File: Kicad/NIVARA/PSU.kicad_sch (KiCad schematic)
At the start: 0 parts

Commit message: Wrapping up for today :3
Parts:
- added C2, C3, C4, C5: C, symbol Device:C
- added L1: L_Ferrite, symbol Device:L_Ferrite
- added U2: AP63203WU, Package_TO_SOT_SMD:TSOT-23-6, symbol Regulator_Switching:AP63203WU
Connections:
- net +3.3V: now also C4.2, C5.2, L1.2, U2.1 (FB)
- new net: C2.1, U2.6 (BST)
- new net: C2.2, L1.1, U2.5 (SW)
- new net GND: C3.1, C4.1, C5.1, U2.4 (GND)
- new net VCC: C3.2, U2.2 (EN), U2.3 (IN)
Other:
- note added: "NOTE: SEE DATASHEET FOR COMPONENT VALUES!!!!"

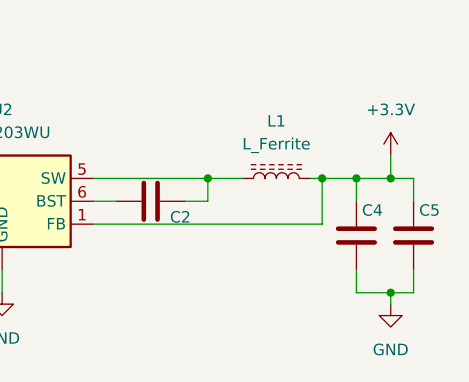
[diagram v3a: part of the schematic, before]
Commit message: Solder Jumper
Para que no me pase lo mismo de mi proyecto
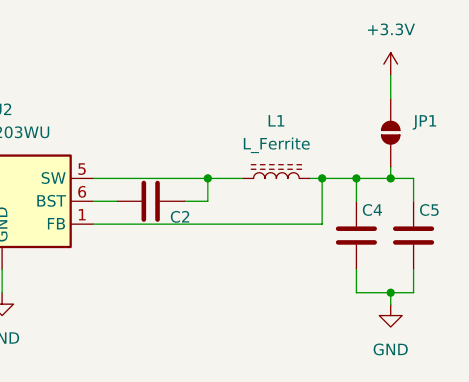
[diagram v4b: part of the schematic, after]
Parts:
- added JP1: SolderJumper_2_Open, Jumper:SolderJumper-2_P1.3mm_Open_RoundedPad1.0x1.5mm, symbol Jumper:SolderJumper_2_Open
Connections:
- net +3.3V: now also JP1.2 (B); no longer C4.2, C5.2, L1.2, U2.1 (FB)
- new net: C4.2, C5.2, JP1.1 (A), L1.2, U2.1 (FB)
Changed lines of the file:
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@@
+	)
+	(junction
+		(at 31.75 40.64)
+		(diameter 0)
+		(color 0 0 0 0)
 	)
 	(junction
@@
 	)
 	(junction
-		(at 31.75 40.64)
-		(diameter 0)
-		(color 0 0 0 0)
-	)
-	(junction
 		(at 36.83 40.64)
 		(diameter 0)
@@
 	(wire
 		(pts
+			(xy 93.98 40.64) (xy 93.98 43.18)
+		)
+		(stroke
+			(width 0)
+			(type default)
+		)
+	)
+	(wire
+		(pts
 			(xy 91.44 40.64) (xy 93.98 40.64)
 		)
@@
 	(wire
 		(pts
-			(xy 93.98 40.64) (xy 93.98 43.18)
-		)
-		(stroke
-			(width 0)
-			(type default)
-		)
-	)
-	(wire
-		(pts
-			(xy 91.44 40.64) (xy 91.44 38.1)
+			(xy 91.44 29.21) (xy 91.44 31.75)
 		)
 		(stroke
@@
 		(pts
 			(xy 58.42 45.72) (xy 83.82 45.72)
+		)
+		(stroke
+			(width 0)
+			(type default)
+		)
+	)
+	(wire
+		(pts
+			(xy 91.44 39.37) (xy 91.44 40.64)
 		)
 		(stroke
@@
 	(symbol
 		(lib_id "power:+3.3V")
-		(at 91.44 38.1 0)
+		(at 91.44 29.21 0)
 		(unit 1)
 		(exclude_from_sim no)
@@
 		(fields_autoplaced yes)
 		(property "Reference" "#PWR01"
-			(at 91.44 41.91 0)
+			(at 91.44 33.02 0)
 			(effects
 				(font
@@
 		)
 		(property "Value" "+3.3V"
-			(at 91.44 33.02 0)
+			(at 91.44 24.13 0)
 			(effects
 				(font
@@
 		)
 		(property "Footprint" ""
-			(at 91.44 38.1 0)
+			(at 91.44 29.21 0)
 			(effects
 				(font
@@
 		)
 		(property "Datasheet" ""
-			(at 91.44 38.1 0)
+			(at 91.44 29.21 0)
 			(effects
 				(font
@@
 		)
 		(property "Description" "Power symbol creates a global label with name \"+3.3V\""
-			(at 91.44 38.1 0)
+			(at 91.44 29.21 0)
 			(effects
 				(font
@@
 					(unit 1)
 				)
+			)
+		)
+	)
+	(symbol
+		(lib_id "Jumper:SolderJumper_2_Open")
+		(at 91.44 35.56 90)
+		(unit 1)
+		(exclude_from_sim no)
+		(in_bom no)
+		(on_board yes)
+		(dnp no)
+		(fields_autoplaced yes)
+		(property "Reference" "JP1"
+			(at 93.98 34.2899 90)
+			(effects
+				(font
+					(size 1.27 1.27)
+				)
+				(justify right)
+			)
+		)
+		(property "Value" "SolderJumper_2_Open"
+			(at 93.98 36.8299 90)
+			(effects
+				(font
+					(size 1.27 1.27)
+				)
+				(justify right)
+				(hide yes)
+			)
+		)
+		(property "Footprint" "Jumper:SolderJumper-2_P1.3mm_Open_RoundedPad1.0x1.5mm"
+			(at 91.44 35.56 0)
+			(effects
+				(font
+					(size 1.27 1.27)
+				)
+				(hide yes)
+			)
+		)
+		(property "Datasheet" "~"
+			(at 91.44 35.56 0)
+			(effects
+				(font
+					(size 1.27 1.27)
+				)
+				(hide yes)
+			)
+		)
+		(property "Description" "Solder Jumper, 2-pole, open"
+			(at 91.44 35.56 0)
+			(effects
+				(font
+					(size 1.27 1.27)
+				)
+				(hide yes)
+			)
+		)
+		(pin "1"
+		)
+		(pin "2"
+		)
+		(instances
+			(project ""
+				(path "/8290cc18-06d0-4e02-a781-29a61ebc321a/9e4d7a0c-a5eb-4e88-9036-0c35e68b279a/8ab7d9d8-a14c-43b1-bf79-ac7dfdaef76f"
+					(reference "JP1")
+					(unit 1)
+				)

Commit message: ZZZ
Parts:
- removed U2: AP63203WU, Package_TO_SOT_SMD:TSOT-23-6, symbol Regulator_Switching:AP63203WU
- added C6: C, symbol Device:C
- added R2, R3: R, symbol Device:R
- added U2: AP63200WU, Package_TO_SOT_SMD:TSOT-23-6, symbol Regulator_Switching:AP63200WU
- C3: Voltage (none) -> 50V
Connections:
- net GND: now also R3.2, U2.4 (GND)
- net VCC: now also U2.2 (EN), U2.3 (IN)
- net at C4.2, C5.2, JP1.1 (A)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: now also C6.1, R2.1
- net at C2.1: now also U2.6 (BST)
- net at C2.2, L1.1: now also U2.5 (SW)
- new net: C6.2, R2.2, R3.1, U2.1 (FB)
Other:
- note added: "AP63200/AP63201 OR AP63203"
- note added: "DO NOT MOUNT FOR AP63203: C6 R3 SUBSITUTE: R2 -> 0Ohm"
- note removed: "NOTE: SEE DATASHEET FOR COMPONENT VALUES!!!!"

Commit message: Rutinario
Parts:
- C2: value C -> 100nF
- C3: value C -> 10uF
- C4, C5: value C -> 22uF
- C6: value C -> 100pF
- L1: value L_Ferrite -> 6.8uH
- R2: value R -> 196k
- R3: value R -> 62k
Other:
- note added: "DO NOT MOUNT FOR AP63203: C6 R3 SUBSITUTE: R2 -> 0Ohm L -> 3.9uH"
- note removed: "DO NOT MOUNT FOR AP63203: C6 R3 SUBSITUTE: R2 -> 0Ohm"

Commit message: FULL SCHEMATIC!!111!!!
Dik
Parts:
- added D6, D7: SMF24A, Diode_SMD:D_SMF, symbol Diode:SMF24A
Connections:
- net GND: now also D6.2 (A2), D7.2 (A2)
- net VCC: now also D7.1 (A1)
- net at C4.2, C5.2, C6.1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: now also D6.1 (A1)

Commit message: Debí de enrutar antes :C
tengo sueño
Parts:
- C2, C3, C4, C5, C6: footprint (none) -> Capacitor_SMD:C_0603_1608Metric
- L1: footprint (none) -> Inductor_SMD:L_6.3x6.3_H3
- R2, R3: footprint (none) -> Resistor_SMD:R_0603_1608Metric
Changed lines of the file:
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@@
 			)
 		)
-		(property "Footprint" ""
+		(property "Footprint" "Capacitor_SMD:C_0603_1608Metric"
 			(at 74.93 50.4952 0)
 			(effects
@@
 			)
 		)
-		(property "Footprint" ""
+		(property "Footprint" "Capacitor_SMD:C_0603_1608Metric"
 			(at 86.6648 43.18 0)
 			(effects
@@
 			)
 		)
-		(property "Footprint" ""
+		(property "Footprint" "Resistor_SMD:R_0603_1608Metric"
 			(at 82.042 66.04 90)
 			(effects
@@
 			)
 		)
-		(property "Footprint" ""
+		(property "Footprint" "Resistor_SMD:R_0603_1608Metric"
 			(at 82.042 55.88 90)
 			(effects
@@
 			)
 		)
-		(property "Footprint" ""
+		(property "Footprint" "Capacitor_SMD:C_0603_1608Metric"
 			(at 68.58 42.2148 0)
 			(effects
@@
 			)
 		)
-		(property "Footprint" ""
+		(property "Footprint" "Capacitor_SMD:C_0603_1608Metric"
 			(at 93.0148 43.18 0)
 			(effects
@@
 			)
 		)
-		(property "Footprint" ""
+		(property "Footprint" "Capacitor_SMD:C_0603_1608Metric"
 			(at 30.7848 43.18 0)
 			(effects
@@
 			)
 		)
-		(property "Footprint" ""
+		(property "Footprint" "Inductor_SMD:L_6.3x6.3_H3"
 			(at 78.74 40.64 0)
 			(effects
